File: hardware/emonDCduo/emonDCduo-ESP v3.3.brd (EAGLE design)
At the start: 16 x 2 mm, 87 parts, among them IC1 ACS758LCB-050B-PFF-T, IC2 ACS758LCB-050B-PFF-T, IC3 LM358D, P1 B4B-PH-K, Y1 32Khz

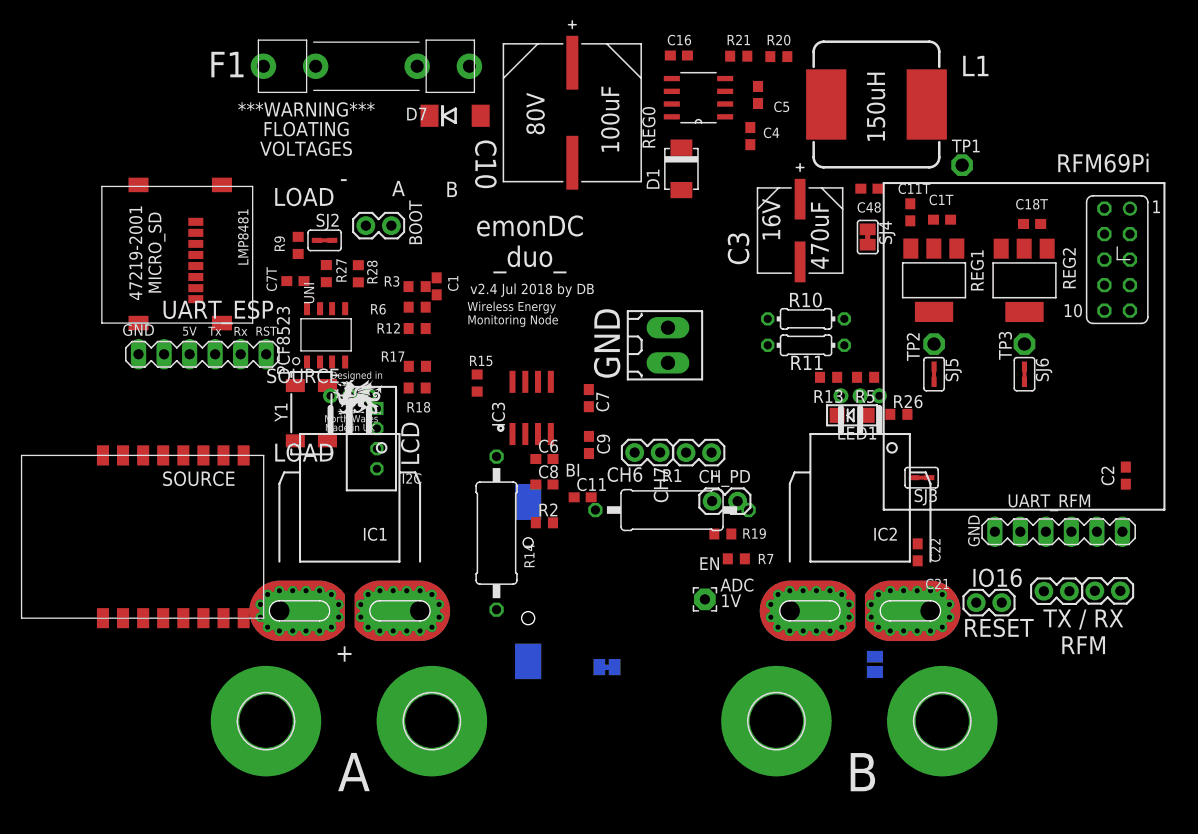
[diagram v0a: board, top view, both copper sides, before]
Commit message: commit v3.3
added temp sensor
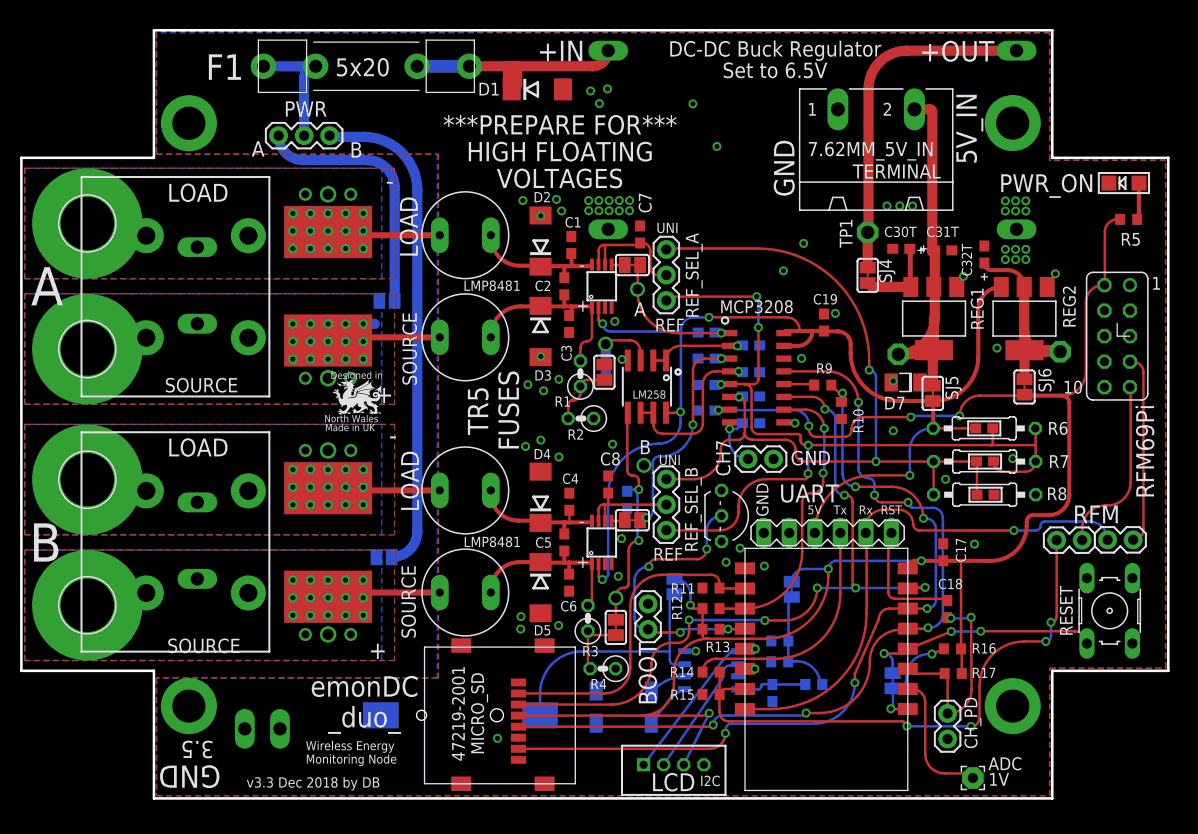
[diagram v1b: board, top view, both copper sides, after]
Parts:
- removed C11T, C18T, C1T: 10uF TANT, rcl:C0603
- removed C22: 100nF, rcl:C0603
- removed C48: 0.1uF, rcl:C0603
- removed C7T: 10uF, rcl@1:C0603
- removed GND: (no value), con-weidmueller-sl35_db:180-2
- removed IC2: ACS758LCB-050B-PFF-T, allegro:CB-PFF
- removed IC3: LM358D, linear:SO08
- removed IO16: FACTORY_RESET, SparkFun:1X02
- removed J1: (no value), SparkFun-Connectors:1X02
- removed L1: SRR1208, inductor-bourns:SSR1208
- removed R18: 2k, rcl:R0603
- removed R19, R28: 10K, rcl:R0603
- removed REG0: MAX5035, MAX5035:21-0111D_SBE-14
- removed UART_ESP: UART_ESP, JeeLabs:MA06-1
- removed UART_RFM: UART_RFM, JeeLabs:MA06-1
- added 7.62MM_5V_IN: GMSTBA2, con-phoenix-762:GMSTBA2
- added C12, C13, C14, C15: 1nF, rcl:C0603
- added C17, C18, C19: 0.1uF, rcl:C0603
- added C20: 1nF 100V, rcl:C0603
- added C30T, C31T, C32T, C33T: 10uF TANT, rcl7:C0603POL
- added D2, D3, D4, D5: P6SMB75A, diode:DO214AA
- added EBW_A, EBW_B: EBW_SERIES_15.2MM, EBW series SHUNT:EBW_SERIES_15.2MM
- added F2, F3, F4, F5: (no value), fuse:TR5
- added LM258: (no value), microbuilder:SOIC8_150MIL
- added MCP3208: MCP3208-BI/SL, MCP3208:SOIC16
- added MOUNT_10.16_A, MOUNT_10.16_B: MOLEX_39970-003, 10.16mm terminal block:2/10,16
- added PWR, REF_SEL_A, REF_SEL_B: 455-1750-1-ND, SparkFun-Connectors:1X03
- added R16: 10K, rcl:R0603
- added R22: 1K, rcl@1:R0603
- added R25: 10k, microbuilder:0603
- added R4: 56K, rcl7:0207/2V
- added R8: 174R, rcl7:0207/10
- added RESET: RESET_BUTT, switch-omron:B3F-10XX
- added SHUNTMON-A, SHUNTMON-B: LMP8481, lmp8481b:S-PDSO-G08
- added SJ1, SJ10, SJ11, SJ8, SJ9: (no value), microbuilder:SOLDERJUMPER_CLOSEDWIRE
- added TP10, TP11, TP12, TP13, TP4, TP5, TP6, TP7, TP8, TP9: TPPAD1-13Y, testpad:P1-13Y
- added U$4, U$5, U$6: TP1.0MM, 1mm tesp pad:TP1.0
- added UART: UART, JeeLabs:MA06-1
- 3.3V_BAT, SJ4: device jumper-con:SJ-CON -> microbuilder:SOLDERJUMPER_CLOSEDWIRE
- C10: value 100uF 80V -> 1nF; device Panasonic-EEE-EEV-EEF-ECQ:CAPAE1350X1400N -> rcl:C0603
- C11, C16: value 0.1uF 100V -> 1nF
- C2, C21: value 100nF -> 1nF 100V
- C3: value 470uF 16V -> 0.1uF 100V; device Panasonic-EEEFK_EEEFP:CAPAE830X1050N -> rcl:C0603
- C4: value 0.1uF 16V -> 0.1uF 100V
- C5: value 0.1uF 16V -> 1nF 100V
- C7: value 0.1uF -> 0.1uF 100V
- C9: value 0.1uF -> 1nF
- D1: value MBRS1100T3G -> P6SMB75A; device diodes:SMB_1 -> diode:DO214AA
- D7: value P6SMB75A -> SMF6.0A; device diode:DO214AA -> smf_10:SOD123F
- IC1: value ACS758LCB-050B-PFF-T -> DS18B20; device allegro:CB-PFF -> DS18B20:TO92-
- LED1: value (none) -> PWR_ON
- R1: value 1.5M 3.5kV -> 1M 100V; device rcl7:0411/15 -> rcl7:0207/2V
- R10: value 16.56k -> 2K; device rcl:0204/7 -> rcl:R0603
- R11: value 5.23k -> 10K; device rcl:0204/7 -> rcl:R0603
- R13: value 5.23k -> 4.7K; device rcl7:R0603 -> rcl:R0603
- R14: value 1.5M 3.5kV -> 1k; device rcl7:0411/15 -> rcl:R0603
- R15: value 100K -> 2k
- R17: value 1k -> 10K
- R2: value 100K -> 56K; device rcl:R0603 -> rcl7:0207/2V
- R20: value 43k -> 10K; device rcl@1:R0603 -> rcl:R0603
- R21: value 10k -> 10K; device rcl@1:R0603 -> rcl:R0603
- R26: value 390R -> 5.6k; device rcl:R0603 -> microbuilder:0603
- R27: value 10K -> 174R; device rcl:R0603 -> microbuilder:0603
- R3: value 10K -> 1M 100V; device rcl:R0603 -> rcl7:0207/2V
- R5: value 517.77k -> 174R; device rcl7:R0603 -> rcl:R0603
- R6: value 10K -> 10k; device rcl:R0603 -> rcl7:0207/10
- R7: value 10K -> 5.6k; device rcl:R0603 -> rcl7:0207/10
- R9: device rcl@1:R0603 -> rcl:R0603
- SJ2, SJ5, SJ6: device jumper-con_db:SJ-CON -> microbuilder:SOLDERJUMPER_CLOSEDWIRE
- SJ3: device jumper-con_db:SJ-CON -> jumper:SJ
- U$1: value (none) -> TP1.0MM; device DRAGON_LOGO:DRAGON_LOGO_NOTEXT -> 1mm tesp pad:TP1.0
- moved MH3 85.9 mm to (0.23, 21.0)
- moved MH4 72.7 mm to (0.23, 33.5)
- moved R27 69.2 mm to (89.6, 32.0), turned to 180 degrees
- moved ESP-12 64.5 mm to (81.9, 26.7), turned to 180 degrees
- moved R17 61.5 mm to (86.4, 14.2)
- moved R21 60.4 mm to (69.1, 15.4), flipped to the bottom
- moved C2 59.0 mm to (47.7, 52.8)
- moved R20 58.2 mm to (69.2, 17.4), flipped to the bottom
- moved SJ2 58.0 mm to (70.3, 22.6), flipped to the bottom, turned to 270 degrees
- moved R6 57.7 mm to (89.5, 38.6)
- moved SJ3 56.0 mm to (30.1, 51.3), flipped to the bottom, turned to 0 degrees
- moved MICRO_SD 56.0 mm to (45.7, 3.24)
- moved R9 54.0 mm to (73.4, 42.9), turned to 0 degrees
- moved MH2 52.6 mm to (0.23, 59.0)
- moved D7 52.1 mm to (81.7, 43.2), turned to 180 degrees
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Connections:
- removed net BST: C4.1, REG0.1
- removed net CH6: J5.2
- removed net LX: C4.2, D1.C, L1.1, REG0.8
- removed net N$20: UART_RFM.5
- removed net N$24: R9.2, SJ2.2
- removed net N$30: C21.2, UART_ESP.1
- removed net N$301: C2.2, UART_RFM.1
- removed net N$6: J1.1
- removed net N$9: IC3.5, R1.1, R2.2
- removed net PRE_6.5V: C3.1, C48.1, L1.2, R20.2, SJ4.1, TP1.TP
- removed net V+: IC3.8
- removed net V-: IC3.4
- removed net VCC_ESP: C22.2, ESP-12.16, R12.2, R19.2, R6.2, R7.2, SJ3.1
- removed net VD: C5.1, REG0.2
- removed net VSENSE_A_BUFF: IC3.1, IC3.2
- removed net VSENSE_B_BUFF: IC3.6, IC3.7
- new net GPIO12A: MCP3208.12, R9.1
- new net LOAD-NEG-A_T: C1.1, C2.1, D2.C, F2.2, SHUNTMON-A.8
- new net LOAD-NEG-B: EBW_A.P$18, EBW_A.P$19, EBW_A.P$2, EBW_A.P$20, EBW_A.P$21, EBW_A.P$22, EBW_A.P$23, EBW_A.P$24, EBW_A.P$25, EBW_A.P$26, EBW_A.P$27, EBW_A.P$28, EBW_A.P$29, EBW_A.P$30, EBW_A.P$31, EBW_A.P$32, EBW_A.P$36, EBW_A.P$37, EBW_A.P$38, F4.1, MH4.B5,5, MOUNT_10.16_B.P$1, MOUNT_10.16_B.P$2, TP9.TP
- new net LOAD-NEG-B_T: C4.1, C5.1, D4.C, F4.2, SHUNTMON-B.8
- new net N$11: SHUNTMON-A.5, SJ11.1
- new net REF_A_INPUT: C7.1, REF_SEL_A.2, SHUNTMON-A.6, SHUNTMON-A.7
- new net REF_B_INPUT: C8.1, REF_SEL_B.2, SHUNTMON-B.6, SHUNTMON-B.7
- new net RESET: C18.2, UART.1
- new net SOURCE-POS-A_T: C2.2, C3.1, D3.C, F3.2, R1.2, SHUNTMON-A.1
- new net SOURCE-POS-B_T: C5.2, C6.1, D5.C, F5.2, R3.2, SHUNTMON-B.1
- new net VDD_PCF: C33T.1, PCF8523.8, R22.1
- new net VDD_RTC_POSTJUMPER: R20.1, R21.1, R22.2, SJ2.2
- new net VSENSE_A_BUFFED: C10.1, LM258.1, LM258.2, MCP3208.2
- new net VSENSE_A_TP: C21.1, LM258.3, SJ8.2, U$1.P$1
- new net VSENSE_B: R3.1, R4.2, SJ9.1
- new net VSENSE_B_BUFFED: C12.1, LM258.6, LM258.7, MCP3208.4
- new net VSENSE_B_TP: C20.1, LM258.5, SJ9.2, U$4.P$1
- net +3V3: now also C15.1, C17.2, ESP-12.16, MCP3208.7, R12.2, R13.2, R16.2, R17.2, R5.2; no longer R26.2, R27.1, R28.1, SJ3.2
- net +5V: now also C19.1, LM258.8, MCP3208.15, MCP3208.16, R25.2, R6.2, SHUNTMON-A.2, SHUNTMON-B.2, UART.4; no longer C1.1, C8.1, IC1.1, IC2.1, R10.2, R5.1, UART_ESP.4, UART_RFM.4
- net 3.3V_PRE: now also C32T.1; no longer C18T.1
- net 5V_PRE: now also 7.62MM_5V_IN.2, C31T.1, D7.C; no longer C1T.1
- net 6.5V: now also C30T.1; no longer C11T.1
- net ADCSHUNT_A: now also C9.1, MCP3208.1, SJ11.2, U$6.P$1; no longer C6.1, IC1.3
- net ADCSHUNT_B: now also MCP3208.3, SJ10.2, U$5.P$1; no longer IC2.3
- net BI_REF: now also C13.1, MCP3208.5, R25.1, R26.2, R6.1, R7.2, REF_SEL_A.3, REF_SEL_B.3; no longer C7.1, R10.1, R11.2
- net CH7: now also C16.1, MCP3208.8
- net CH_PD: now also C18.1, R17.1; no longer C21.1, R7.1
- net D0/RX: no longer UART_RFM.2
- net D1/TX: no longer UART_RFM.3
- net ESPRX: now also R14.2, R15.1; no longer R17.2, R18.1
- net ESPTX: now also UART.2; no longer UART_ESP.2
- net GND: now also 7.62MM_5V_IN.1, C17.1, C19.2, C30T.2, C31T.2, C32T.2, C33T.2, C4.2, D2.A, D3.A, D4.A, D5.A, IC1.1, IC1.3, J5.2, LM258.4, MCP3208.14, MCP3208.9, R10.2, R11.2, R15.2, R27.1, R4.1, R8.1, RESET.3, SHUNTMON-A.4, SHUNTMON-B.4, TP12.TP, TP13.TP, TP6.TP, TP7.TP, UART.6; no longer C10.2, C11.2, C11T.2, C16.2, C18T.2, C1T.2, C22.1, C48.2, C5.2, C7T.2, C9.2, GND.1, GND.2, IC1.2, IC2.2, IO16.2, R11.1, R13.2, R15.1, R18.2, R21.1, R3.2, REG0.3, REG0.6, UART_ESP.6, UART_RFM.6
- net GPIO0: now also IC1.2, R13.1; no longer R12.1
- net GPIO12: now also R10.1, R9.2
- net GPIO13: now also MCP3208.11
- net GPIO14: now also MCP3208.13
- net GPIO15: now also R11.1; no longer R3.1
- net GPIO16: now also RESET.1, SJ1.2; no longer IO16.1, SJ7.1
- net GPIO2: now also MCP3208.10, R12.1; no longer R6.1
- net LOAD-NEG-A: now also EBW_B.P$18, EBW_B.P$19, EBW_B.P$2, EBW_B.P$20, EBW_B.P$21, EBW_B.P$22, EBW_B.P$23, EBW_B.P$24, EBW_B.P$25, EBW_B.P$26, EBW_B.P$27, EBW_B.P$28, EBW_B.P$29, EBW_B.P$30, EBW_B.P$31, EBW_B.P$32, EBW_B.P$36, EBW_B.P$37, EBW_B.P$38, F2.1, MOUNT_10.16_A.P$1, MOUNT_10.16_A.P$2, TP11.TP; no longer IC1.IP+, IC1.IP+@10, IC1.IP+@11, IC1.IP+@12, IC1.IP+@13, IC1.IP+@14, IC1.IP+@15, IC1.IP+@16, IC1.IP+@17, IC1.IP+@2, IC1.IP+@3, IC1.IP+@4, IC1.IP+@5, IC1.IP+@6, IC1.IP+@7, IC1.IP+@8, IC1.IP+@9
- net N$1: now also SJ4.1, TP1.TP, TP5.TP; no longer R20.1, R21.2, REG0.4
- net N$10: now also SHUNTMON-B.5, SJ10.1; no longer C7T.1, PCF8523.8, R9.1
- net N$3: now also PWR.3, SJ3.1; no longer IC2.IP+, IC2.IP+@10, IC2.IP+@11, IC2.IP+@12, IC2.IP+@13, IC2.IP+@14, IC2.IP+@15, IC2.IP+@16, IC2.IP+@17, IC2.IP+@2, IC2.IP+@3, IC2.IP+@4, IC2.IP+@5, IC2.IP+@6, IC2.IP+@7, IC2.IP+@8, IC2.IP+@9, MH4.B5,5
- net N$36: now also R14.1, UART.3; no longer R17.1, UART_ESP.3
- net N$4: now also PWR.1, SJ7.2; no longer J1.2
- net N$5: now also R5.1; no longer R26.1
- net RST: now also R16.1, SJ1.1; no longer R19.1, SJ7.2
- net SCL: no longer R27.2
- net SDA: no longer R28.2
- net SOURCE-POS-A: now also EBW_B.P$1, EBW_B.P$10, EBW_B.P$11, EBW_B.P$12, EBW_B.P$13, EBW_B.P$14, EBW_B.P$15, EBW_B.P$16, EBW_B.P$17, EBW_B.P$3, EBW_B.P$33, EBW_B.P$34, EBW_B.P$35, EBW_B.P$4, EBW_B.P$5, EBW_B.P$6, EBW_B.P$7, EBW_B.P$8, EBW_B.P$9, F3.1, MOUNT_10.16_A.P$3, MOUNT_10.16_A.P$4, SJ3.2, TP10.TP; no longer IC1.IP-, IC1.IP-@10, IC1.IP-@11, IC1.IP-@12, IC1.IP-@13, IC1.IP-@14, IC1.IP-@15, IC1.IP-@16, IC1.IP-@17, IC1.IP-@2, IC1.IP-@3, IC1.IP-@4, IC1.IP-@5, IC1.IP-@6, IC1.IP-@7, IC1.IP-@8, IC1.IP-@9, R14.2
- net SOURCE-POS-B: now also EBW_A.P$1, EBW_A.P$10, EBW_A.P$11, EBW_A.P$12, EBW_A.P$13, EBW_A.P$14, EBW_A.P$15, EBW_A.P$16, EBW_A.P$17, EBW_A.P$3, EBW_A.P$33, EBW_A.P$34, EBW_A.P$35, EBW_A.P$4, EBW_A.P$5, EBW_A.P$6, EBW_A.P$7, EBW_A.P$8, EBW_A.P$9, F5.1, MOUNT_10.16_B.P$3, MOUNT_10.16_B.P$4, SJ7.1, TP8.TP; no longer IC2.IP-, IC2.IP-@10, IC2.IP-@11, IC2.IP-@12, IC2.IP-@13, IC2.IP-@14, IC2.IP-@15, IC2.IP-@16, IC2.IP-@17, IC2.IP-@2, IC2.IP-@3, IC2.IP-@4, IC2.IP-@5, IC2.IP-@6, IC2.IP-@7, IC2.IP-@8, IC2.IP-@9, R1.2
- net UNI_REF: now also C14.1, MCP3208.6, R26.1, R27.2, R7.1, R8.2, REF_SEL_A.1, REF_SEL_B.1; no longer C9.1, R13.1, R5.2
- net VSENSE_A: now also R1.1, R2.2, SJ8.1; no longer IC3.3, R14.1, R15.2
- net V_IN_POSTFUSE: now also D1.C, TP4.TP; no longer C10.1, C16.1, D7.C, REG0.5, REG0.7
- net V_IN_PREFUSE: now also PWR.2
- net _RESET: no longer C2.1
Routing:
- net +3V3: track 0.00 -> 172.8 mm, vias 0 -> 8
- net +5V: track 0.00 -> 114.8 mm, vias 0 -> 5
- net BI_REF: track 0.00 -> 85.7 mm, vias 0 -> 5
- net GPIO14: track 0.00 -> 82.9 mm, vias 0 -> 6
- net UNI_REF: track 0.00 -> 81.3 mm, vias 0 -> 3
- net GPIO12: track 0.00 -> 79.3 mm, vias 0 -> 6
- net GPIO13: track 0.00 -> 71.7 mm, vias 0 -> 7
- net 5V_PRE: track 0.00 -> 56.9 mm
- net ESPRX: track 0.00 -> 55.8 mm, vias 0 -> 4
- net ESPTX: track 0.00 -> 51.4 mm, vias 0 -> 1
- net N$4: track 0.00 -> 48.5 mm
- net 3.3V_PRE: track 0.00 -> 37.4 mm
- net N$1: track 0.00 -> 34.1 mm
- net GPIO15: track 0.00 -> 31.9 mm
- net GPIO0: track 0.00 -> 28.7 mm, vias 0 -> 4
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- added copper zone on layer 1, net GND
- added copper zone on layer 16, net GND
- added copper zone on layer 1, net LOAD-NEG-A
- added copper zone on layer 16, net LOAD-NEG-A
- added copper zone on layer 1, net LOAD-NEG-B
- added copper zone on layer 16, net LOAD-NEG-B
- added copper zone on layer 1, net SOURCE-POS-A
- added copper zone on layer 16, net SOURCE-POS-A
- added copper zone on layer 1, net SOURCE-POS-B
- added copper zone on layer 16, net SOURCE-POS-B
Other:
- board size 16 x 2 mm -> 114.2 x 76.5 mm
- board text added: "***PREPARE FOR*** HIGH FLOATING VOLTAGES"
- board text added: "+IN"
- board text added: "+OUT"
- board text added: "3.5"
- board text added: "5V_IN"
- board text added: "5x20"
- board text added: "DC-DC Buck Regulator Set to 6.5V"
- board text added: "Designed in North Wales by Daniel Bates"
- board text added: "Open Hardware"
- board text added: "PWR_ON"
- board text added: "REF"
- board text added: "RFM"
- board text added: "TERMINAL"
- board text added: "TR5 FUSES"
- board text added: "v3.3 Dec 2018 by DB"
- board text removed: "***WARNING*** FLOATING VOLTAGES"
- board text removed: "100uF"
- board text removed: "150uH"
- board text removed: "16V"
- board text removed: "470uF"
- board text removed: "80V"
- board text removed: "BI"
- board text removed: "CH6"
- board text removed: "Designed in North Wales UK by Daniel Bates"
- board text removed: "EN"
- board text removed: "Open-Hardware"
- board text removed: "RESET"
- board text removed: "TX / RX RFM"
- board text removed: "v2.4 Jul 2018 by DB"
